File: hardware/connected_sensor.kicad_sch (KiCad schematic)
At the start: 43 parts, among them J1 Conn_01x04, J2 Conn_01x04, J3 Conn_01x05, J4 Conn_01x05, J5 Conn_01x03, J6 AC_IN, J7 LOAD, J8 UEXT, K1 G2RL-1A-E 5DC, M1 ESP8266-DEV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

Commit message: Note P/N for current transformer
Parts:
- T1: P/N (none) -> CSE187L-P
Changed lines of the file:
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@@
+      (effects (font (size 1.27 1.27)) hide)
+    )
+    (property "P/N" "CSE187L-P" (id 4) (at 161.29 151.13 0)
       (effects (font (size 1.27 1.27)) hide)
     )

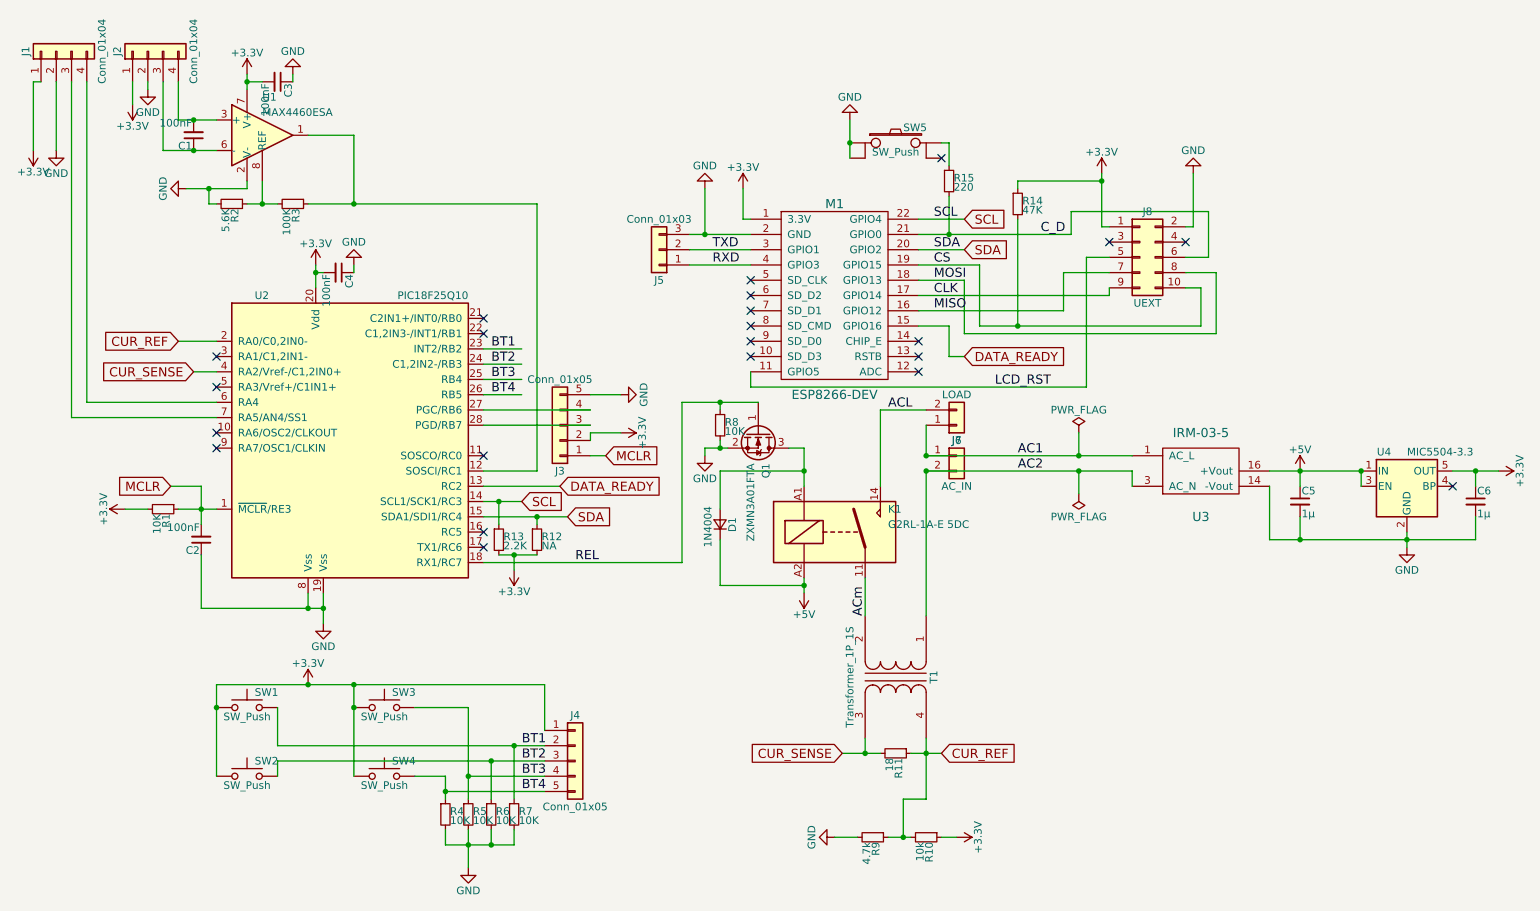
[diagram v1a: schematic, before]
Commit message: Add surge protections on current sensor
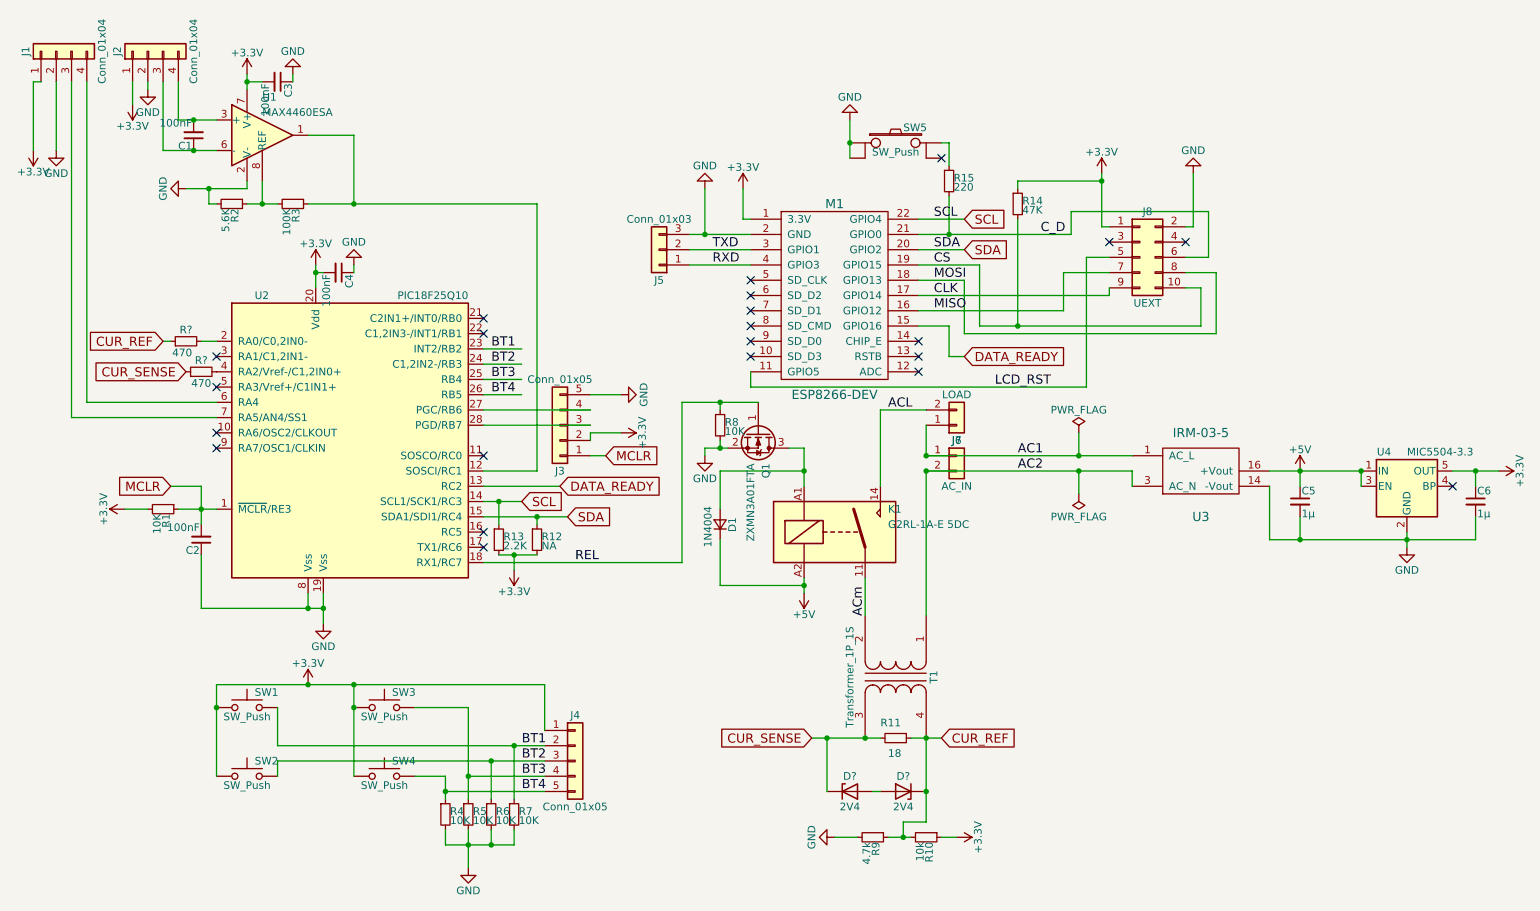
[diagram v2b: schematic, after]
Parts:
- added D? (x2): 2V4, symbol Device:D_Zener
- added R? (x2): 470, symbol Device:R_Small
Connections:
- net CUR_REF: now also D?.1 (K), R?.1; no longer U2.2 (RA0/C0,2IN0-)
- net CUR_SENSE: now also D?.1 (K), R?.1; no longer U2.4 (RA2/Vref-/C1,2IN0+)
- new net: R?.2, U2.2 (RA0/C0,2IN0-)
- new net: R?.2, U2.4 (RA2/Vref-/C1,2IN0+)
- new net: D?.2 (A), D?.2 (A)
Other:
- moved on the sheet: R11
